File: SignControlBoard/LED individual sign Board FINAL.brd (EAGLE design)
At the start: 35.4 x 31.7 mm, 25 parts, among them U1 ATMEGA328P, U2 M5205 5v, X1 22-23-2021, Y1 16MHz

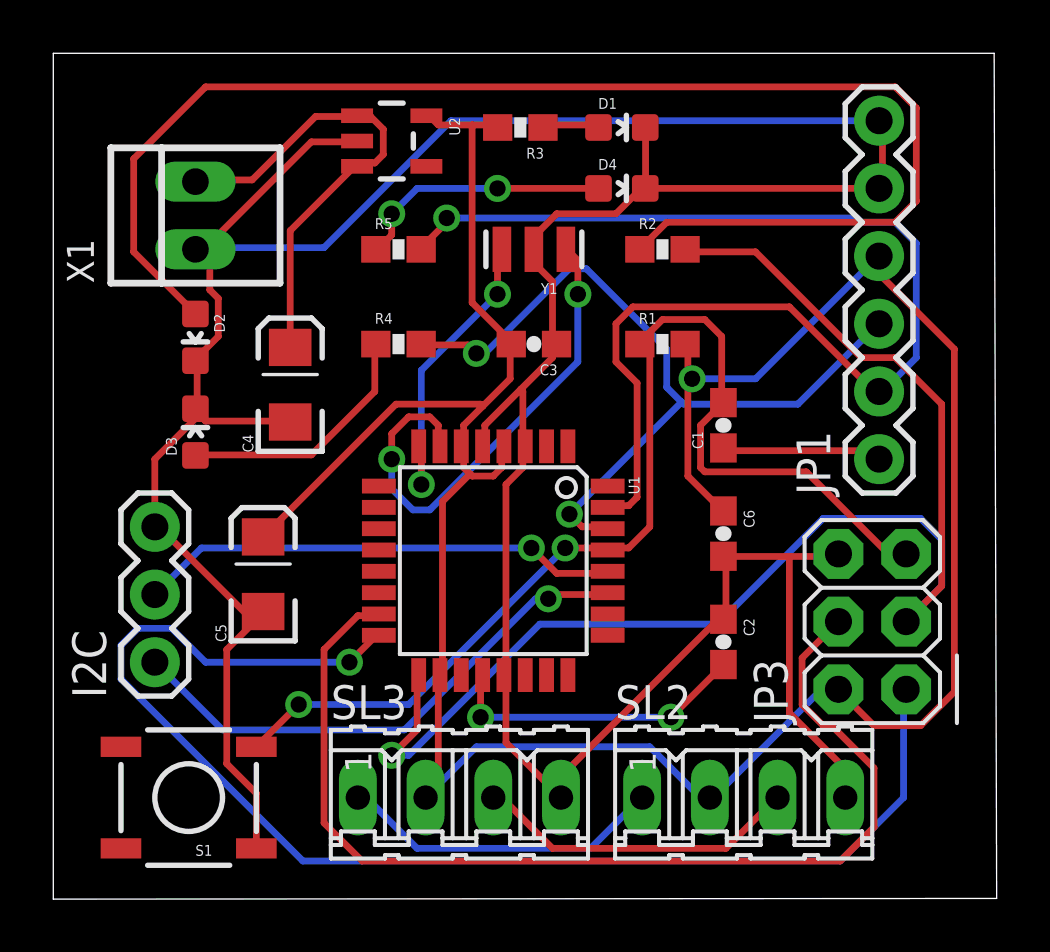
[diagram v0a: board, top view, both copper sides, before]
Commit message: Made traces on power thicker
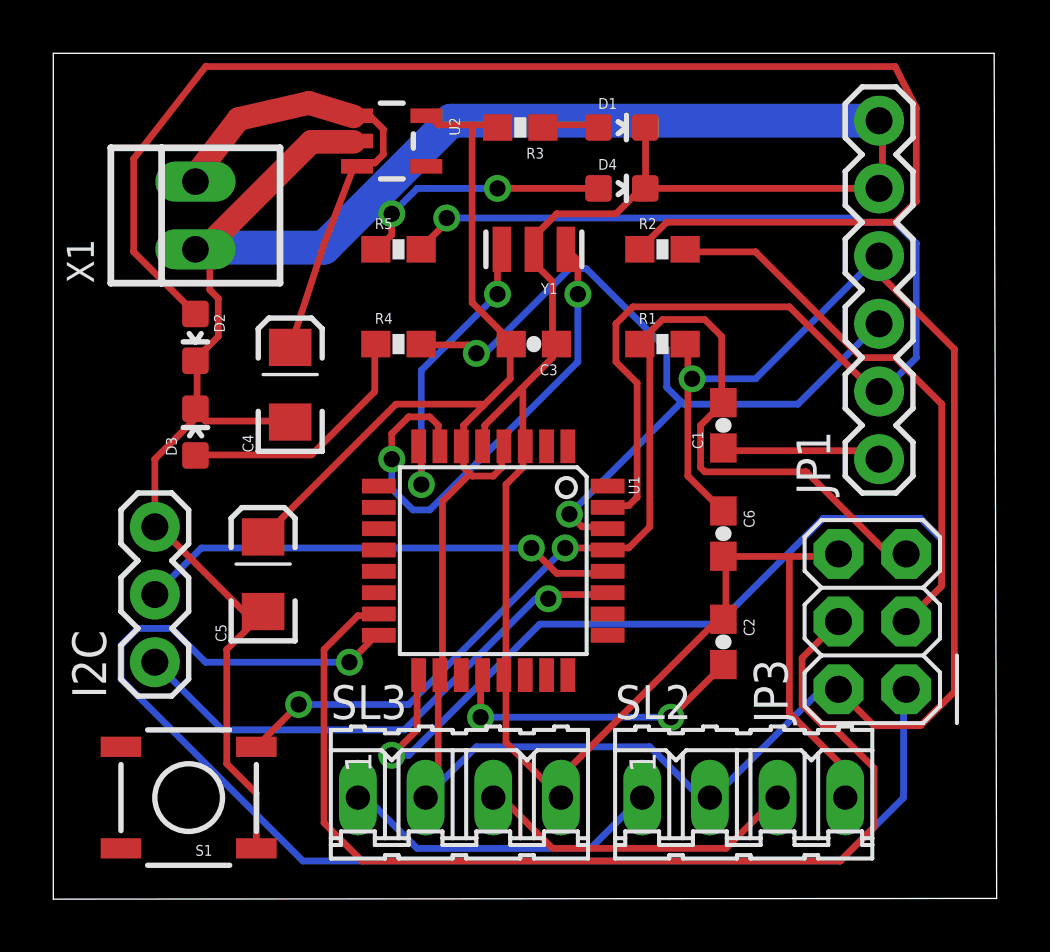
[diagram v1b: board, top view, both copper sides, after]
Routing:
- net N$4: track 52.2 -> 53.4 mm
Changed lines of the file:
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@@
 <contactref element="SL3" pad="4"/>
 <contactref element="X1" pad="1"/>
-<wire x1="9.68375" y1="28.41625" x2="11.27125" y2="28.41625" width="0.254" layer="1"/>
-<wire x1="5.715" y1="24.4475" x2="9.68375" y2="28.41625" width="0.254" layer="1"/>
+<wire x1="9.68375" y1="28.41625" x2="11.27125" y2="28.41625" width="0.889" layer="1"/>
+<wire x1="5.715" y1="24.4475" x2="9.68375" y2="28.41625" width="0.889" layer="1"/>
 <wire x1="5.3975" y1="24.4475" x2="5.715" y2="24.4475" width="0.254" layer="1"/>
 <wire x1="11.27125" y1="28.41625" x2="11.3999" y2="28.448" width="0.254" layer="1"/>
-<wire x1="5.3975" y1="24.4475" x2="5.334" y2="24.384" width="0.254" layer="1"/>
+<wire x1="5.3975" y1="24.4475" x2="5.334" y2="24.384" width="0.889" layer="1"/>
 <wire x1="7.62" y1="3.96875" x2="7.62" y2="1.905" width="0.254" layer="1"/>
 <wire x1="6.50875" y1="5.08" x2="7.62" y2="3.96875" width="0.254" layer="1"/>
@@
 <wire x1="16.98625" y1="8.41375" x2="16.91" y2="8.4074" width="0.254" layer="1"/>
 <wire x1="17.62125" y1="16.98625" x2="17.71" y2="16.9926" width="0.254" layer="1"/>
-<wire x1="10.16" y1="24.4475" x2="5.3975" y2="24.4475" width="0.254" layer="16"/>
-<wire x1="14.9225" y1="29.21" x2="10.16" y2="24.4475" width="0.254" layer="16"/>
-<wire x1="30.988" y1="29.21" x2="14.9225" y2="29.21" width="0.254" layer="16"/>
+<wire x1="10.16" y1="24.4475" x2="5.3975" y2="24.4475" width="1.27" layer="16"/>
+<wire x1="14.9225" y1="29.21" x2="10.16" y2="24.4475" width="1.27" layer="16"/>
+<wire x1="30.988" y1="29.21" x2="14.9225" y2="29.21" width="1.27" layer="16"/>
 <wire x1="5.3975" y1="24.4475" x2="5.334" y2="24.384" width="0.254" layer="16"/>
 </signal>
@@
 <wire x1="11.43" y1="27.6225" x2="11.3999" y2="27.498" width="0.254" layer="1"/>
 <wire x1="11.43" y1="29.36875" x2="11.3999" y2="29.398" width="0.254" layer="1"/>
-<wire x1="8.89" y1="25.0825" x2="8.89" y2="20.704" width="0.254" layer="1"/>
-<wire x1="11.27125" y1="27.46375" x2="8.89" y2="25.0825" width="0.254" layer="1"/>
+<wire x1="10.16" y1="24.5745" x2="8.89" y2="20.704" width="0.254" layer="1"/>
+<wire x1="11.27125" y1="27.46375" x2="10.16" y2="24.5745" width="0.254" layer="1"/>
 <wire x1="11.27125" y1="27.46375" x2="11.3999" y2="27.498" width="0.254" layer="1"/>
-<wire x1="7.46125" y1="26.9875" x2="5.3975" y2="26.9875" width="0.254" layer="1"/>
-<wire x1="9.8425" y1="29.36875" x2="7.46125" y2="26.9875" width="0.254" layer="1"/>
-<wire x1="11.27125" y1="29.36875" x2="9.8425" y2="29.36875" width="0.254" layer="1"/>
-<wire x1="5.3975" y1="26.9875" x2="5.334" y2="26.924" width="0.254" layer="1"/>
+<wire x1="6.95325" y1="29.2735" x2="5.3975" y2="27.2415" width="0.889" layer="1"/>
+<wire x1="9.5885" y1="29.87675" x2="6.95325" y2="29.2735" width="0.889" layer="1"/>
+<wire x1="11.27125" y1="29.36875" x2="9.5885" y2="29.87675" width="0.889" layer="1"/>
+<wire x1="5.3975" y1="27.2415" x2="5.334" y2="26.924" width="0.889" layer="1"/>
 <wire x1="11.27125" y1="29.36875" x2="11.3999" y2="29.398" width="0.254" layer="1"/>
 </signal>
@@
 <wire x1="3.01625" y1="24.28875" x2="5.23875" y2="22.06625" width="0.254" layer="1"/>
 <wire x1="3.01625" y1="27.78125" x2="3.01625" y2="24.28875" width="0.254" layer="1"/>
-<wire x1="5.715" y1="30.48" x2="3.01625" y2="27.78125" width="0.254" layer="1"/>
-<wire x1="31.59125" y1="30.48" x2="5.715" y2="30.48" width="0.254" layer="1"/>
-<wire x1="32.385" y1="29.68625" x2="31.59125" y2="30.48" width="0.254" layer="1"/>
+<wire x1="5.715" y1="31.242" x2="3.01625" y2="27.78125" width="0.254" layer="1"/>
+<wire x1="31.59125" y1="31.242" x2="5.715" y2="31.242" width="0.254" layer="1"/>
+<wire x1="32.385" y1="29.68625" x2="31.59125" y2="31.242" width="0.254" layer="1"/>
 <wire x1="32.385" y1="26.19375" x2="32.385" y2="29.68625" width="0.254" layer="1"/>
 <wire x1="31.59125" y1="25.4" x2="32.385" y2="26.19375" width="0.254" layer="1"/>
